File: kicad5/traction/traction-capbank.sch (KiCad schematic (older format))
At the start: 26 parts

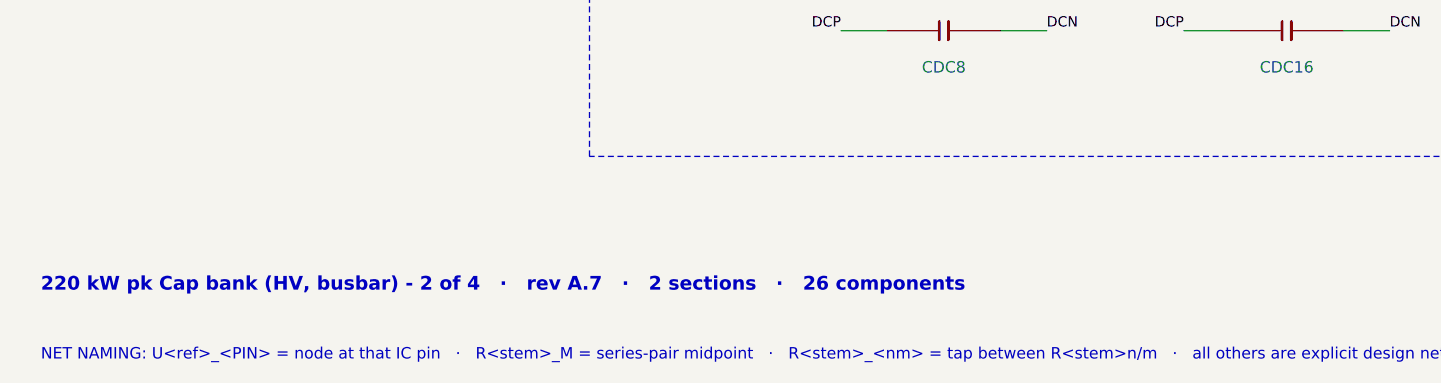
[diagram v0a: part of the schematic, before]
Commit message: Rev A.8: review round 8 response (R7-01..07, A7-N01..05) + cross-check
Review round 8 on 2ac42ed, every finding verified and classified in
docs/review-A8-disposition.md (+ .csv); findings log F90-F105.

Hardware (+Rs18/unit: SiC Rs71,040, IGBT Rs45,540):
- UASCG 74LVC1G08-Q100: ASC_CMD = ASC latch AND no driver FLT, so a
  latched DESAT drops ASC on every path, FS1B included (R7-01/A7-N01;
  NSI6611 DS Fig. 8.11 read directly)
- USCH2 74LVC3G17-Q100 buffers both latch presets and drives QDIS_CMD;
  FLT diode-OR now BAT46 for the Schmitt threshold (R7-02, R7-03, N12)
- ZSET BZT52-B5V6 to ground replaces the clamp into V5A; RENP2 removed
  (A7-N04; B5V6 keeps a 35 V load dump under the 6.5 V V_I abs max)
- RASCL = RQDL = 261 R: both TLP152 LEDs 10.3-14.8 mA, inside 10-15 mA
- dead-state pulls: RFCB on FLT_CMB_B, RASCP moved to ASC_Q
- CFLTF2 100 pF on FLT_LS_N; discharge header V15-GND-CMD-GND

Firmware contract: FW-15 always clears the ASC latch; FW-16 runs on
measured no-HV/standstill conditions (stored-pass arming otherwise),
handles the FS_GPIO1 flyback OR and injects FLT from the MCU pins;
FW-08b; FS1B_TDELAY = 0, TDUR = 100 ms; FAULT_OUT outcomes stated.

Tooling: ERC locks by net, pin number and first-match MPN per SKU
(864 checks, each new one mutation-tested); computed judges replace
fixed PASS rows; S4 static junction path + static-plate bound; VCC2
FB-sense per corner; bom-gen publishes atomically, rounds ext prices.

Gates: pins 1782/1782, ERC 864/0, design-verify 108P/14W/0F,
sim-verify 23P/6W/0F, marine 81P/19W/0F.

Co-Authored-By: Claude Opus 5.5 <noreply@anthropic.com>
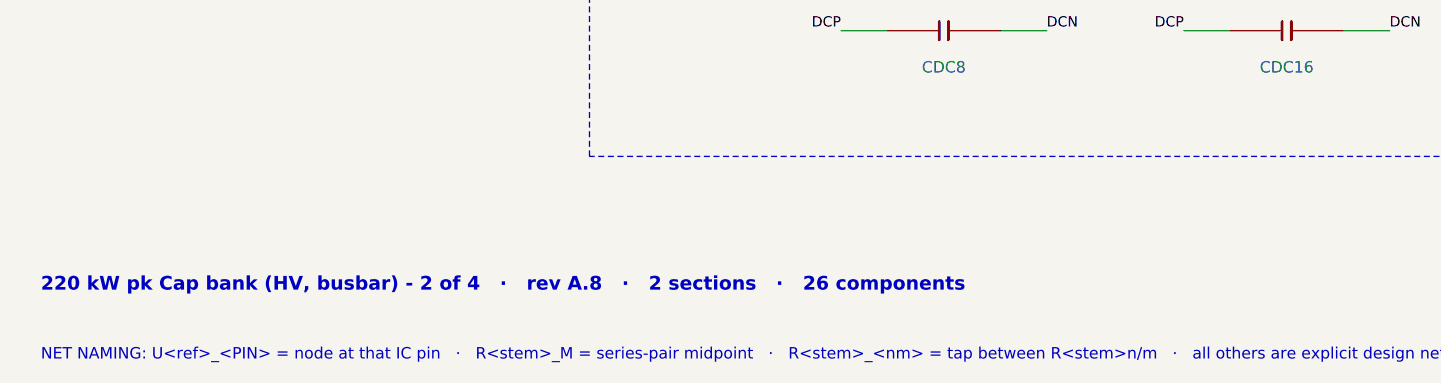
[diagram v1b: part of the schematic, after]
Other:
- note added: "220 kW pk Cap bank (HV, busbar) - 2 of 4 · rev A.8 · 2 sections · 26 components"
- note removed: "220 kW pk Cap bank (HV, busbar) - 2 of 4 · rev A.7 · 2 sections · 26 components"
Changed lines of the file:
@@
 Title "Traction Inverter — Cap bank (busbar assembly, 320 uF)"
 Date "2026-09-23"
-Rev "A.7"
+Rev "A.8"
 Comp "Traction Inverter 220 kW pk - Cap bank (HV, busbar), sheet 2 of 4"
 Comment1 "Inverter = Power board + Cap bank busbar + bolt-on Discharge board (all HV) + Control card (LV); safe state holds with any link lost"
@@
 $EndDescr
 Text Notes 600 5100 0    60   ~ 12
-220 kW pk Cap bank (HV, busbar) - 2 of 4   ·   rev A.7   ·   2 sections   ·   26 components
+220 kW pk Cap bank (HV, busbar) - 2 of 4   ·   rev A.8   ·   2 sections   ·   26 components
 Text Notes 600 5400 0    50   ~ 0
 NET NAMING: U<ref>_<PIN> = node at that IC pin   ·   R<stem>_M = series-pair midpoint   ·   R<stem>_<nm> = tap between R<stem>n/m   ·   all others are explicit design nets   ·   same name on another sheet = same net, joined only at the named connector/stud/tab

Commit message: Rev A.9: review round 9 response (A8-01..03, A8-N01..N03) + cross-check
Review round 9 on 0da9014, every finding verified and classified in
docs/review-A9-disposition.md (+ .csv, 34 items); findings log F106-F119.

Hardware (+Rs29/unit: SiC Rs71,069, IGBT Rs45,569):
- PSASC/PSQD bound to the real QA01C-18 sheet (+18/-3 V; F61 had read
  the base QA01C, +20/-4 V): envelope 16.9-20.9 V, ASC entry 7.52 us,
  FW-06 end-point 906 V; discharge gate divider RQDG 1.5k (Vgs 13.4-18.1 V)
- FLT/RDY pull-ups and the diode-OR pull-up moved to V5GD (the drivers'
  VCC1; FLT/RDY abs max = VCC1), V5GD read by the MCU on PTB5
- HARNESS40 re-laid: VBAT and V5GD touch only ground in both row-by-row
  and odd/even dual-row numbering; connector family chosen at layout
- self-found: the power board's LV side ran on unswitched KL30
  (~150 mA parked) - card-side P-FET switch DMP6023LEQ on V5A with a
  slew network; resolver LDO enabled by V5A; parking drain <= 43 uA
- RFS4 = ROHM ESR03 anti-surge; CASC/CQD 50 V

Firmware contract: FW-16 energy-limited eligibility (read < 3 V or QDIS
for 2 tau); V_DC invalid while V5GD is out of window; DESATs to NVM;
BACKUP_SAFETY_PATH_FS1B = 0; motor/vehicle release rule for SPO energy.

Gates: pins 1804/1804, ERC 883/0 (new locks mutation-tested),
design-verify 116P/14W/0F, sim-verify 23P/6W/0F, marine 81P/19W/0F.

Co-Authored-By: Claude Opus 5.5 <noreply@anthropic.com>
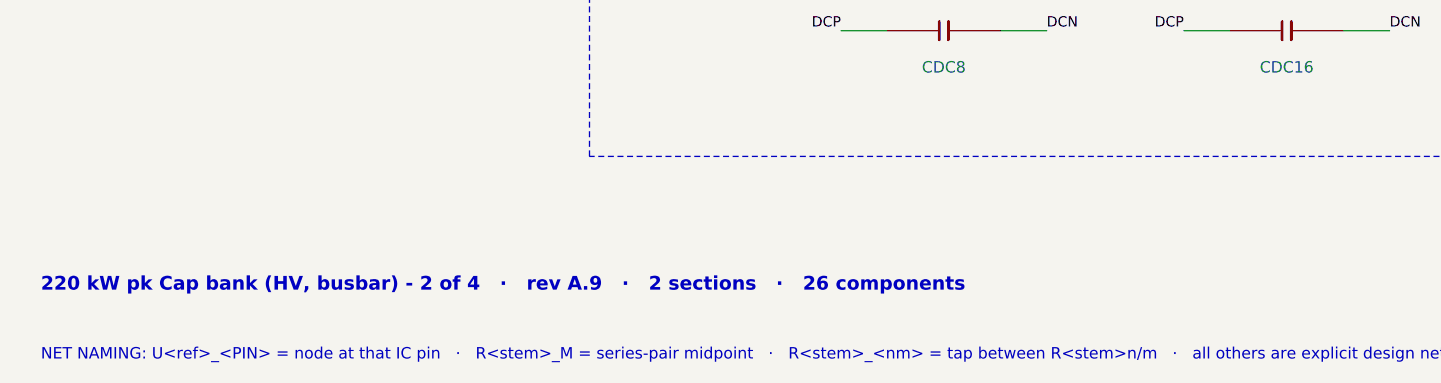
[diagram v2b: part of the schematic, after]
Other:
- note added: "220 kW pk Cap bank (HV, busbar) - 2 of 4 · rev A.9 · 2 sections · 26 components"
- note removed: "220 kW pk Cap bank (HV, busbar) - 2 of 4 · rev A.8 · 2 sections · 26 components"
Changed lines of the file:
@@
 Title "Traction Inverter — Cap bank (busbar assembly, 320 uF)"
 Date "2026-09-23"
-Rev "A.8"
+Rev "A.9"
 Comp "Traction Inverter 220 kW pk - Cap bank (HV, busbar), sheet 2 of 4"
 Comment1 "Inverter = Power board + Cap bank busbar + bolt-on Discharge board (all HV) + Control card (LV); safe state holds with any link lost"
@@
 $EndDescr
 Text Notes 600 5100 0    60   ~ 12
-220 kW pk Cap bank (HV, busbar) - 2 of 4   ·   rev A.8   ·   2 sections   ·   26 components
+220 kW pk Cap bank (HV, busbar) - 2 of 4   ·   rev A.9   ·   2 sections   ·   26 components
 Text Notes 600 5400 0    50   ~ 0
 NET NAMING: U<ref>_<PIN> = node at that IC pin   ·   R<stem>_M = series-pair midpoint   ·   R<stem>_<nm> = tap between R<stem>n/m   ·   all others are explicit design nets   ·   same name on another sheet = same net, joined only at the named connector/stud/tab

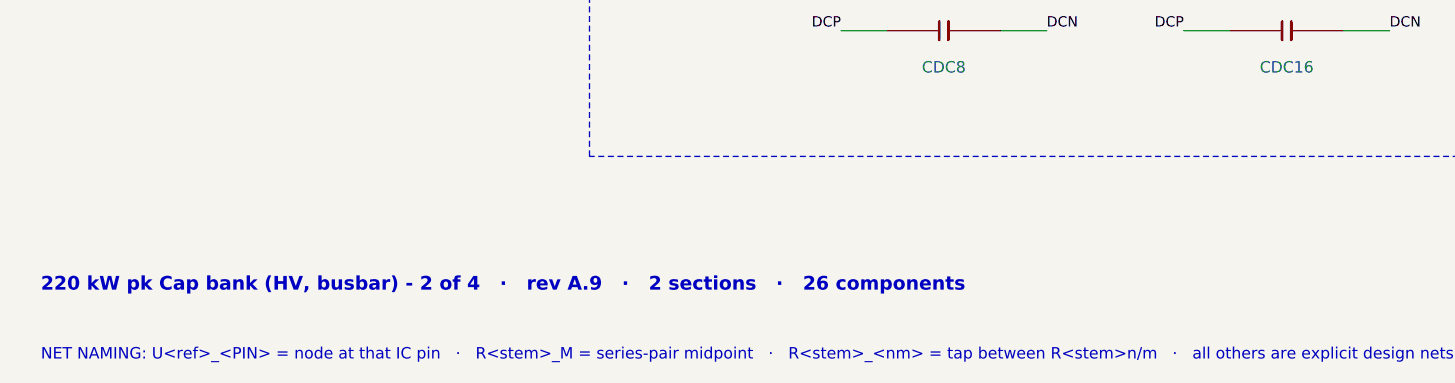
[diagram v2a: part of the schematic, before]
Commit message: Rev A.10: schematic rechecks of A.9 (A9-S01, S9-01, S9-02)
Two schematic-only rechecks of 7235337 kept every A.9 correction;
dispositioned in docs/review-A10-disposition.md (+ .csv); F120-F122.

- RDY_HS/RDY_LS now reach UAND1/UAND2 through a third 74LVC3G17-Q100
  (USCH3, RRDB dead-state pull-down): the open-drain lines rose at
  ~20-100 ns/V against the 74LVC1G11's 10 ns/V limit (A9-S01; reverses
  the round-7/8 "state-benign" rejection)
- RASCG = ROHM ESR03EZPF2201 (0.27 W at 85 C): it carries up to 0.12 W
  for as long as ASC is held; 2.2 k kept for the ASC timing (S9-01)
- discharge sheet note 66k bleeder; gate divider stated as 13.3-18.2 V
  (a divider, not a clamp); A9 disposition quotes the final harness map

+Rs11/unit (SiC Rs71,080, IGBT Rs45,580).
Gates: pins 1815/1815, ERC 891/0 (new locks mutation-tested),
design-verify 118P/14W/0F, sim-verify 23P/6W/0F, marine 81P/19W/0F.

Co-Authored-By: Claude Opus 5.5 <noreply@anthropic.com>
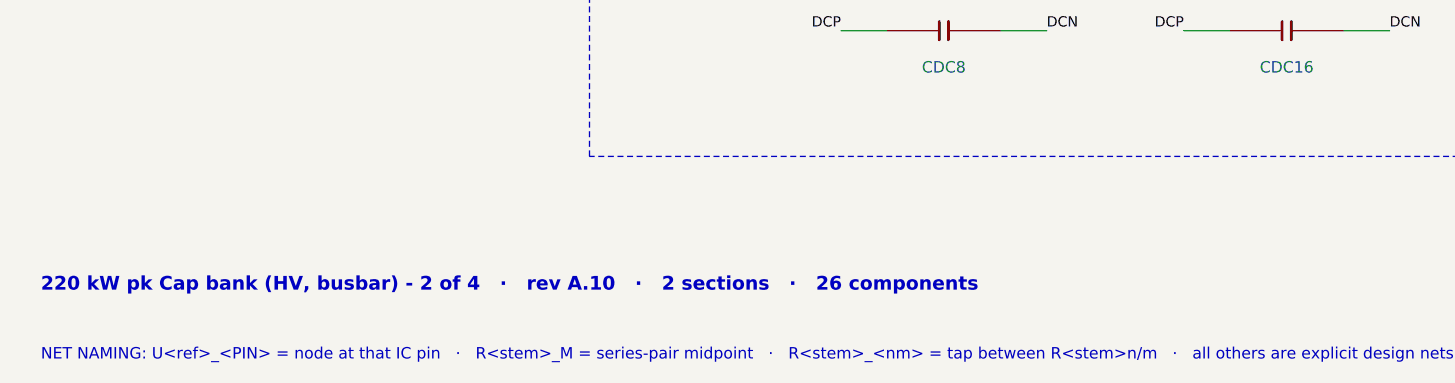
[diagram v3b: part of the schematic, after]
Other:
- note added: "220 kW pk Cap bank (HV, busbar) - 2 of 4 · rev A.10 · 2 sections · 26 components"
- note removed: "220 kW pk Cap bank (HV, busbar) - 2 of 4 · rev A.9 · 2 sections · 26 components"
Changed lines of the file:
@@
 Title "Traction Inverter — Cap bank (busbar assembly, 320 uF)"
 Date "2026-09-23"
-Rev "A.9"
+Rev "A.10"
 Comp "Traction Inverter 220 kW pk - Cap bank (HV, busbar), sheet 2 of 4"
 Comment1 "Inverter = Power board + Cap bank busbar + bolt-on Discharge board (all HV) + Control card (LV); safe state holds with any link lost"
@@
 $EndDescr
 Text Notes 600 5100 0    60   ~ 12
-220 kW pk Cap bank (HV, busbar) - 2 of 4   ·   rev A.9   ·   2 sections   ·   26 components
+220 kW pk Cap bank (HV, busbar) - 2 of 4   ·   rev A.10   ·   2 sections   ·   26 components
 Text Notes 600 5400 0    50   ~ 0
 NET NAMING: U<ref>_<PIN> = node at that IC pin   ·   R<stem>_M = series-pair midpoint   ·   R<stem>_<nm> = tap between R<stem>n/m   ·   all others are explicit design nets   ·   same name on another sheet = same net, joined only at the named connector/stud/tab

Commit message: Rev A.11: review round 12 response (R1-F01..F28, R2-F01..F35) + datasheet archive
Two whole-system reviews of 4544715 (28 + 35 findings), dispositioned line by
line in docs/review-A11-disposition.md (+ CSV). Twelve real findings fixed
(F123-F134); the rest are tracked gates, firmware-owned, wording or out of the
schematic release's scope. No power-stage, capacitor or topology change.

Hardware / contract:
- SS6 release rule (a) is an energy inequality: winding energy 1.5*L*I^2 plus the
  back-EMF work during the decay, closed-form screen while E < V0, diode-bridge
  simulation otherwise; screening rows (WARN) per SKU
- Resolver exciter rewired as a textbook MFB (1.5 nF / 220 pF): the drawn network
  had the feedback pair swapped, |H(10 kHz)| 0.18 -> 1.85; SWG given its 47 pF load
- V_DC bias: "MGJ2D150505SC" was not an existing order code and no MGJ2 is
  reinforced above 150 Vrms -> TI UCC12050 per channel (V_IOWM 1200 Vrms /
  1697 VDC) behind its own NCV4276C from V15
- Hall: 100 k pull-downs drawn (claimed since A.4); LEM HC5FW drawn with its
  real terminals (1 V_ref, 2 V_out, 3 Gnd, 4 U_C, E1-E4)
- Resolver inputs 10 k / 10 k with rescaled, symmetric filter caps: a wire shorted
  to KL30 injected 23 mA into an SDADC pin against the 3 mA limit
- LV-entry TVS bound explicitly as TPSMC24CA-VR (24 V stand-off, AEC-Q101): the
  classic part the notes described conducts at a 24 V jump start; the OEM's
  load-dump source resistance becomes gate 23
- CSB5 1 uF 0805 (VREF5 inside the FS26 window), ALM2402 as HTSSOP14-PWP,
  on-board NTCs RTAMB/RTHS, kicad5-verify empty-set guard
- Contract wording: FW-05 in instantaneous amperes with a validity window, the
  "BMS limit 0" row split from "contactor open", NVM logging queued behind the
  safe action, FW-02 tau check demoted to plausibility (EOL measurement in dfm),
  FW-18 "unknown, never safe", S6 double-update stated; stale pin-40 / LQFP-176 /
  "inside 6 us" / ALT-field texts corrected; CAN termination DNP option

Doc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
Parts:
- removed JCBDN, JCBDP: STUD-M6, StudM6, symbol traction-r1:TERM_1
- removed JCBEN, JCBEP: STUD-M8, StudM8, symbol traction-r1:TERM_1
- removed JCBUN, JCBUP, JCBVN: TAB-M6, TabM6, symbol traction-r1:TERM_1
- added CDC3, CDC4, CDC5, CDC6, CDC7, CDC8, CDC9: 20uF, FilmCan37.5, symbol traction-r1:C
- JCBDN: renamed from JCBVP; value TAB-M6 -> STUD-M6; footprint TabM6 -> StudM6; MPN TAB-M6 -> STUD-M6
- JCBDP: renamed from JCBWN; value TAB-M6 -> STUD-M6; footprint TabM6 -> StudM6; MPN TAB-M6 -> STUD-M6
- JCBEN: renamed from JCBWP; value TAB-M6 -> STUD-M8; footprint TabM6 -> StudM8; MPN TAB-M6 -> STUD-M8
- JCBEP: renamed from CDC1; value 20uF -> STUD-M8; footprint FilmCan37.5 -> StudM8; symbol traction-r1:C -> traction-r1:TERM_1; LCSC C2840809 -> CLASS; MPN C3D1M206KFSA382 -> STUD-M8
- JCBUN: renamed from CDC10; value 20uF -> TAB-M6; footprint FilmCan37.5 -> TabM6; symbol traction-r1:C -> traction-r1:TERM_1; LCSC C2840809 -> CLASS; MPN C3D1M206KFSA382 -> TAB-M6
- JCBUP: renamed from CDC11; value 20uF -> TAB-M6; footprint FilmCan37.5 -> TabM6; symbol traction-r1:C -> traction-r1:TERM_1; LCSC C2840809 -> CLASS; MPN C3D1M206KFSA382 -> TAB-M6
- JCBVN: renamed from CDC12; value 20uF -> TAB-M6; footprint FilmCan37.5 -> TabM6; symbol traction-r1:C -> traction-r1:TERM_1; LCSC C2840809 -> CLASS; MPN C3D1M206KFSA382 -> TAB-M6
- JCBVP: renamed from CDC13; value 20uF -> TAB-M6; footprint FilmCan37.5 -> TabM6; symbol traction-r1:C -> traction-r1:TERM_1; LCSC C2840809 -> CLASS; MPN C3D1M206KFSA382 -> TAB-M6
- JCBWN: renamed from CDC14; value 20uF -> TAB-M6; footprint FilmCan37.5 -> TabM6; symbol traction-r1:C -> traction-r1:TERM_1; LCSC C2840809 -> CLASS; MPN C3D1M206KFSA382 -> TAB-M6
- JCBWP: renamed from CDC15; value 20uF -> TAB-M6; footprint FilmCan37.5 -> TabM6; symbol traction-r1:C -> traction-r1:TERM_1; LCSC C2840809 -> CLASS; MPN C3D1M206KFSA382 -> TAB-M6
- renumbered CDC16 to CDC1, CDC2 to CDC10, CDC3 to CDC11, CDC4 to CDC12, CDC5 to CDC13, CDC6 to CDC14, CDC7 to CDC15, CDC8 to CDC16, CDC9 to CDC2
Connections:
- net DCN: now also JCBDN.1 (P), JCBEN.1 (P), JCBUN.1 (P), JCBVN.1 (P), JCBWN.1 (P), CDC3.2, CDC4.2, CDC5.2, CDC6.2, CDC7.2, CDC8.2, CDC9.2; no longer JCBDP.1 (P), JCBEP.2, JCBUN.2, JCBUP.2, JCBVN.2, JCBVP.2, JCBWN.2, JCBWP.2
- net DCP: now also JCBDP.1 (P), CDC3.1, CDC4.1, CDC5.1, CDC6.1, CDC7.1, CDC8.1, CDC9.1; no longer JCBDN.1 (P), JCBEN.1 (P), JCBUN.1, JCBVN.1, JCBWN.1
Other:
- note added: "220 kW pk Cap bank (HV, busbar) - 2 of 4 · rev A.11 · 2 sections · 26 components"
- note removed: "220 kW pk Cap bank (HV, busbar) - 2 of 4 · rev A.10 · 2 sections · 26 components"
- moved on the sheet: CDC1, CDC10, CDC11, CDC12, CDC13, CDC14, CDC15, CDC16, CDC2, JCBDN, JCBDP, JCBEN
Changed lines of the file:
@@
 Title "Traction Inverter — Cap bank (busbar assembly, 320 uF)"
 Date "2026-09-23"
-Rev "A.10"
+Rev "A.11"
 Comp "Traction Inverter 220 kW pk - Cap bank (HV, busbar), sheet 2 of 4"
 Comment1 "Inverter = Power board + Cap bank busbar + bolt-on Discharge board (all HV) + Control card (LV); safe state holds with any link lost"
@@
 $EndDescr
 Text Notes 600 5100 0    60   ~ 12
-220 kW pk Cap bank (HV, busbar) - 2 of 4   ·   rev A.10   ·   2 sections   ·   26 components
+220 kW pk Cap bank (HV, busbar) - 2 of 4   ·   rev A.11   ·   2 sections   ·   26 components
 Text Notes 600 5400 0    50   ~ 0
 NET NAMING: U<ref>_<PIN> = node at that IC pin   ·   R<stem>_M = series-pair midpoint   ·   R<stem>_<nm> = tap between R<stem>n/m   ·   all others are explicit design nets   ·   same name on another sheet = same net, joined only at the named connector/stud/tab
@@
 $Comp
 L traction-r1:TERM_1 JCBDN
-U 1 1 5E000133
+U 1 1 5E00013A
 P 1250 2350
 F 0 "JCBDN" H 1250 2190 50  0000 C CNN
@@
 $Comp
 L traction-r1:TERM_1 JCBDP
-U 1 1 5E000134
+U 1 1 5E00013B
 P 1250 1950
 F 0 "JCBDP" H 1250 1790 50  0000 C CNN
@@
 $Comp
 L traction-r1:TERM_1 JCBEN
-U 1 1 5E000135
+U 1 1 5E00013C
 P 1250 1550
 F 0 "JCBEN" H 1250 1390 50  0000 C CNN
@@
 $Comp
 L traction-r1:TERM_1 JCBEP
-U 1 1 5E000136
+U 1 1 5E00013D
 P 1250 1150
 F 0 "JCBEP" H 1250 990 50  0000 C CNN
@@
 $Comp
 L traction-r1:TERM_1 JCBUN
-U 1 1 5E000137
+U 1 1 5E00013E
 P 2150 1550
 F 0 "JCBUN" H 2150 1390 50  0000 C CNN
@@
 $Comp
 L traction-r1:TERM_1 JCBUP
-U 1 1 5E000138
+U 1 1 5E00013F
 P 2150 1150
 F 0 "JCBUP" H 2150 990 50  0000 C CNN
@@
 $Comp
 L traction-r1:TERM_1 JCBVN
-U 1 1 5E000139
+U 1 1 5E000140
 P 2150 2350
 F 0 "JCBVN" H 2150 2190 50  0000 C CNN
@@
 $Comp
 L traction-r1:TERM_1 JCBVP
-U 1 1 5E00013A
+U 1 1 5E000141
 P 2150 1950
 F 0 "JCBVP" H 2150 1790 50  0000 C CNN
@@
 $Comp
 L traction-r1:TERM_1 JCBWN
-U 1 1 5E00013B
+U 1 1 5E000142
 P 2150 3150
 F 0 "JCBWN" H 2150 2990 50  0000 C CNN
@@
 $Comp
 L traction-r1:TERM_1 JCBWP
-U 1 1 5E00013C
+U 1 1 5E000143
 P 2150 2750
 F 0 "JCBWP" H 2150 2590 50  0000 C CNN
@@
 $Comp
 L traction-r1:C CDC1
-U 1 1 5E00013D
+U 1 1 5E000144
 P 4550 1150
 F 0 "CDC1" H 4550 990 50  0000 C CNN
@@
 $Comp
 L traction-r1:C CDC10
-U 1 1 5E00013E
+U 1 1 5E000145
 P 6050 1550
 F 0 "CDC10" H 6050 1390 50  0000 C CNN
@@
 $Comp
 L traction-r1:C CDC11
-U 1 1 5E00013F
+U 1 1 5E000146
 P 6050 1950
 F 0 "CDC11" H 6050 1790 50  0000 C CNN
@@
 $Comp
 L traction-r1:C CDC12
-U 1 1 5E000140
+U 1 1 5E000147
 P 6050 2350
 F 0 "CDC12" H 6050 2190 50  0000 C CNN
@@
 $Comp
 L traction-r1:C CDC13
-U 1 1 5E000141
+U 1 1 5E000148
 P 6050 2750
 F 0 "CDC13" H 6050 2590 50  0000 C CNN
@@
 $Comp
 L traction-r1:C CDC14
-U 1 1 5E000142
+U 1 1 5E000149
 P 6050 3150
 F 0 "CDC14" H 6050 2990 50  0000 C CNN
@@
 $Comp
 L traction-r1:C CDC15
-U 1 1 5E000143
+U 1 1 5E00014A
 P 6050 3550
 F 0 "CDC15" H 6050 3390 50  0000 C CNN
@@
 $Comp
 L traction-r1:C CDC16
-U 1 1 5E000144
+U 1 1 5E00014B
 P 6050 3950
 F 0 "CDC16" H 6050 3790 50  0000 C CNN
@@
 $Comp
 L traction-r1:C CDC2
-U 1 1 5E000145
+U 1 1 5E00014C
 P 4550 1550
 F 0 "CDC2" H 4550 1390 50  0000 C CNN
@@
 $Comp
 L traction-r1:C CDC3
-U 1 1 5E000146
+U 1 1 5E00014D
 P 4550 1950
 F 0 "CDC3" H 4550 1790 50  0000 C CNN
@@
 $Comp
 L traction-r1:C CDC4
-U 1 1 5E000147
+U 1 1 5E00014E
 P 4550 2350
 F 0 "CDC4" H 4550 2190 50  0000 C CNN
@@
 $Comp
 L traction-r1:C CDC5
-U 1 1 5E000148
+U 1 1 5E00014F
 P 4550 2750
 F 0 "CDC5" H 4550 2590 50  0000 C CNN
@@
 $Comp
 L traction-r1:C CDC6
-U 1 1 5E000149
+U 1 1 5E000150
 P 4550 3150
 F 0 "CDC6" H 4550 2990 50  0000 C CNN
@@
 $Comp
 L traction-r1:C CDC7
-U 1 1 5E00014A
+U 1 1 5E000151
 P 4550 3550
 F 0 "CDC7" H 4550 3390 50  0000 C CNN
@@
 $Comp
 L traction-r1:C CDC8
-U 1 1 5E00014B
+U 1 1 5E000152
 P 4550 3950
 F 0 "CDC8" H 4550 3790 50  0000 C CNN
@@
 $Comp
 L traction-r1:C CDC9
-U 1 1 5E00014C
+U 1 1 5E000153
 P 6050 1150
 F 0 "CDC9" H 6050 990 50  0000 C CNN
